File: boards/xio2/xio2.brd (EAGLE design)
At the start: 170 x 100 mm, 330 parts, among them J1 12401598E4#2A, Q1 BSS138, Q2 BSS138, Q3 BC817-16LT3G, Q4 BC817-16LT3G, X1 MINI-USB-UX60-MB-5ST, Y2 NX3225SA-12.000MHZ-STD-CSR-1

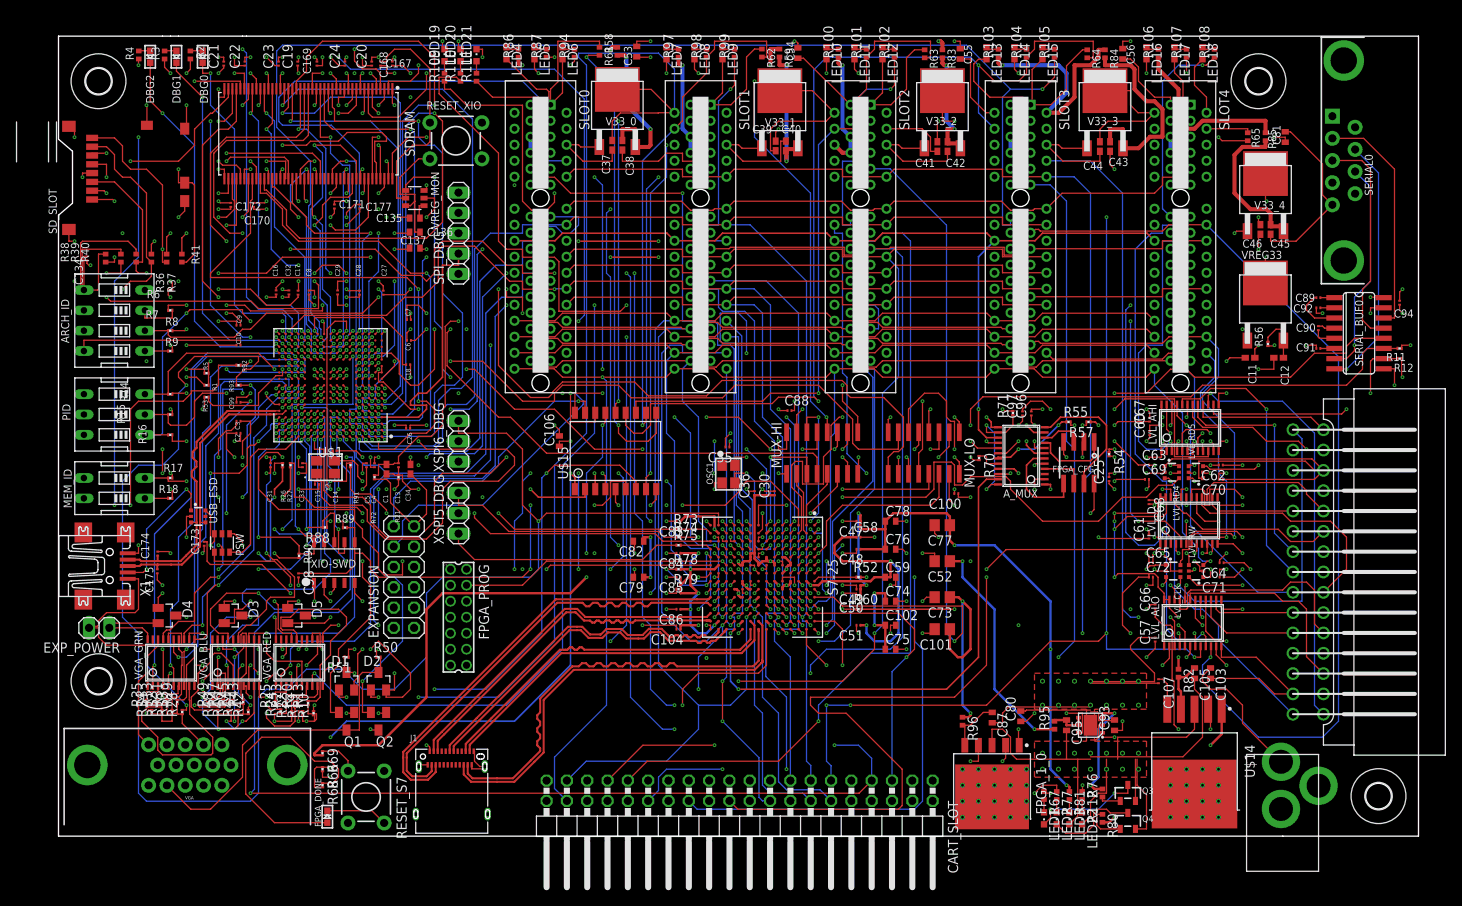
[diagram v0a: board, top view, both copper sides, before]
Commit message: Add slot signals between slots 1&2 and 3&4. Grounds on S5 Add capacitor to VBUS Removed the old annotations Changed resistors for STM debug leds Add pull-ups on TMDS inputs (TX lines on this schematic) Added ‘misc’ line to USB interface. Not high-speed.
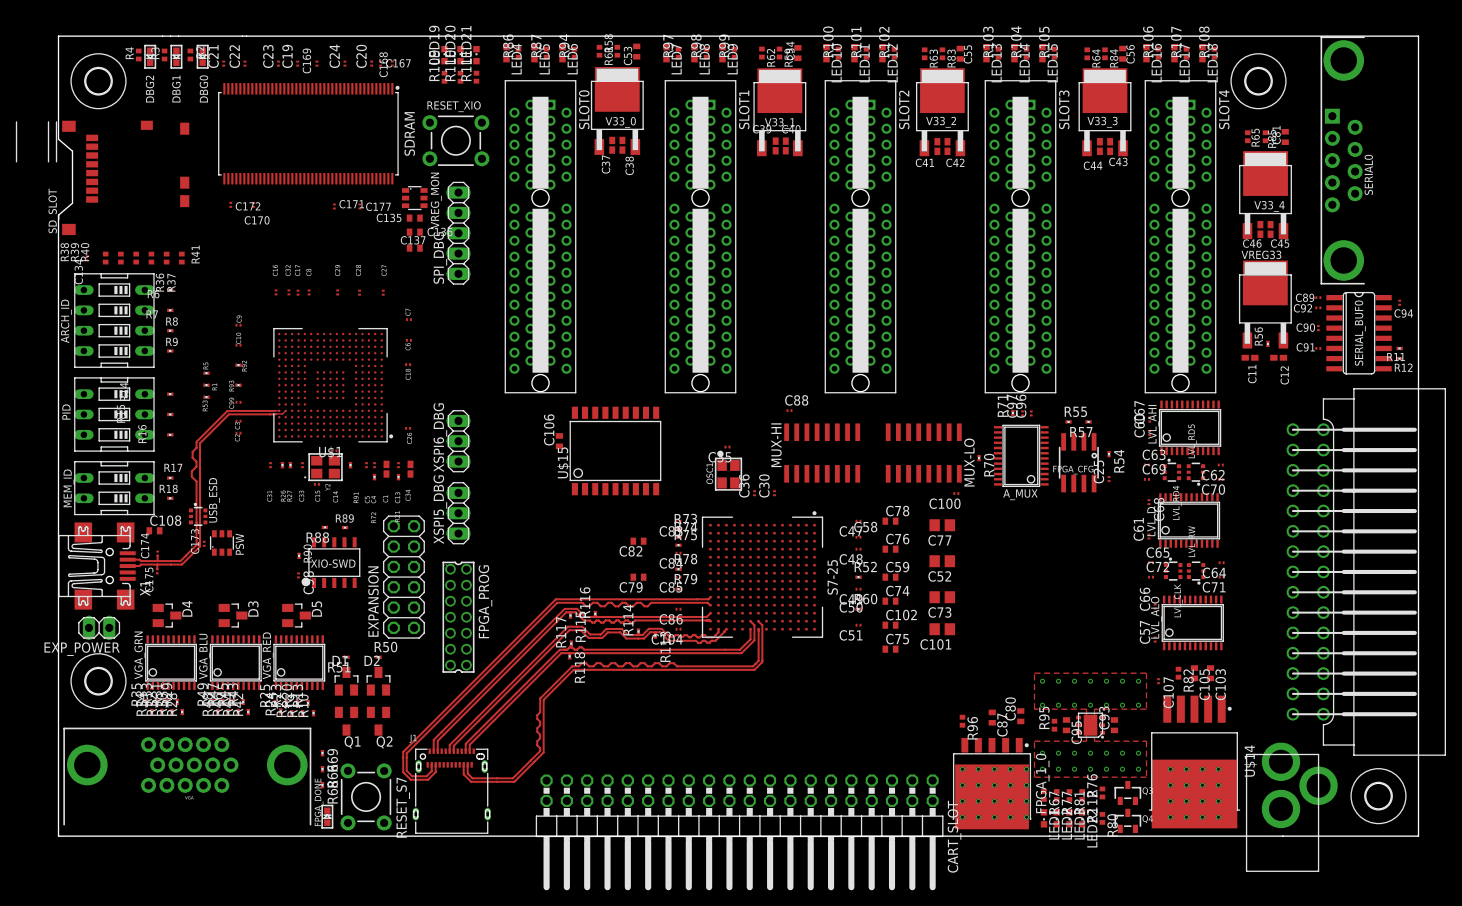
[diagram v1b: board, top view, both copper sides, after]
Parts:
- added C108: 4.7uF, rcl:C0402
- added R113, R114, R115, R116, R117, R118: 50R, rcl:R0201
- R2, R3, R4: value 1K -> 130R
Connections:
- new net LX_MISC: J1.A5, S7-25.M10
- new net SBUS12_CTL0: SLOT0.B8, SLOT1.B8
- new net SBUS12_CTL1: SLOT0.B9, SLOT1.B9
- new net SBUS12_CTL2: SLOT0.B10, SLOT1.B10
- new net SBUS12_CTL3: SLOT0.B11, SLOT1.B11
- new net SBUS12_CTL4: SLOT0.B12, SLOT1.B12
- new net SBUS12_D0: SLOT0.B18, SLOT1.B18
- new net SBUS12_D1: SLOT0.B19, SLOT1.B19
- new net SBUS12_D2: SLOT0.B20, SLOT1.B20
- new net SBUS12_D3: SLOT0.B21, SLOT1.B21
- new net SBUS12_D4: SLOT0.B22, SLOT1.B22
- new net SBUS12_D5: SLOT0.B23, SLOT1.B23
- new net SBUS12_D6: SLOT0.B24, SLOT1.B24
- new net SBUS12_D7: SLOT0.B25, SLOT1.B25
- new net SBUS34_CTL0: SLOT2.B8, SLOT3.B8
- new net SBUS34_CTL1: SLOT2.B9, SLOT3.B9
- new net SBUS34_CTL2: SLOT2.B10, SLOT3.B10
- new net SBUS34_CTL3: SLOT2.B11, SLOT3.B11
- new net SBUS34_CTL4: SLOT2.B12, SLOT3.B12
- new net SBUS34_D0: SLOT2.B18, SLOT3.B18
- new net SBUS34_D1: SLOT2.B19, SLOT3.B19
- new net SBUS34_D2: SLOT2.B20, SLOT3.B20
- new net SBUS34_D3: SLOT2.B21, SLOT3.B21
- new net SBUS34_D4: SLOT2.B22, SLOT3.B22
- new net SBUS34_D5: SLOT2.B23, SLOT3.B23
- new net SBUS34_D6: SLOT2.B24, SLOT3.B24
- new net SBUS34_D7: SLOT2.B25, SLOT3.B25
- net GND: now also C108.2, SLOT4.B10, SLOT4.B11, SLOT4.B12, SLOT4.B18, SLOT4.B19, SLOT4.B20, SLOT4.B21, SLOT4.B22, SLOT4.B23, SLOT4.B24, SLOT4.B25, SLOT4.B8, SLOT4.B9
- net LX_TC_N: now also R113.1
- net LX_TC_P: now also R114.1
- net LX_TD0_N: now also R115.1
- net LX_TD0_P: now also R116.1
- net LX_TD1_N: now also R117.1
- net LX_TD1_P: now also R118.1
- net VCCO: now also R113.2, R114.2, R115.2, R116.2, R117.2, R118.2
- net XIO_USB_VBUS: now also C108.1
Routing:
- net GND: track 970.2 -> 0.00 mm, vias 355 -> 64
- net +5V: track 683.6 -> 0.00 mm, vias 42 -> 0
- net HOST_A3: track 359.3 -> 0.00 mm, vias 7 -> 0
- net HOST_A15: track 345.9 -> 0.00 mm, vias 6 -> 0
- net +3V3: track 335.4 -> 0.00 mm, vias 138 -> 0
- net HOST_A7: track 316.5 -> 0.00 mm, vias 3 -> 0
- net HOST_A0: track 307.0 -> 0.00 mm, vias 5 -> 0
- net HOST_A1: track 294.7 -> 0.00 mm, vias 5 -> 0
- net HOST_A4: track 289.7 -> 0.00 mm, vias 5 -> 0
- net HOST_A6: track 279.7 -> 0.00 mm, vias 3 -> 0
- net SPI_CLK: track 278.7 -> 0.00 mm, vias 7 -> 0
- net HOST_A5: track 274.6 -> 0.00 mm, vias 7 -> 0
- net HOST_A11: track 265.5 -> 0.00 mm, vias 6 -> 0
- net HOST_A2: track 262.9 -> 0.00 mm, vias 6 -> 0
- net VCCO: track 261.9 -> 0.00 mm, vias 20 -> 0
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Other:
- board text removed: "USB3 connector uses milling layer for oval hole. Check this is valid"

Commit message: Change the input clock to 25MHz for STM. This is based on STM32Cube calculations
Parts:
- C14, C15: value 12pF -> 16pF
- Y2: value NX3225SA-12.000MHZ-STD-CSR-1 -> FA-238 25.0000MB-K3
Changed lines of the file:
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@@
 <attribute name="VALUE" x="43.95" y="46.5" size="1.016" layer="27" rot="R90"/>
 </element>
-<element name="Y2" library="microbuilder" package="CRYSTAL_3.2X2.5" value="NX3225SA-12.000MHZ-STD-CSR-1" x="33.3825" y="46.755" smashed="yes">
+<element name="Y2" library="microbuilder" package="CRYSTAL_3.2X2.5" value="FA-238 25.0000MB-K3" x="33.3825" y="46.755" smashed="yes">
 <attribute name="NAME" x="33.36925" y="44.73075" size="0.6096" layer="25" ratio="20" rot="R270"/>
 <attribute name="VALUE" x="31.4775" y="44.596" size="0.4064" layer="27" ratio="10"/>
 </element>
-<element name="C14" library="rcl" library_urn="urn:adsk.eagle:library:334" package="C0201" package3d_urn="urn:adsk.eagle:package:23690/2" value="12pF" x="34.5" y="48.8" smashed="yes">
+<element name="C14" library="rcl" library_urn="urn:adsk.eagle:library:334" package="C0201" package3d_urn="urn:adsk.eagle:package:23690/2" value="16pF" x="34.5" y="48.8" smashed="yes">
 <attribute name="NAME" x="34.93875" y="42.3" size="0.6096" layer="25" ratio="20" rot="R90"/>
 <attribute name="SPICEPREFIX" value="C" x="34.5" y="48.8" size="1.778" layer="27" display="off"/>
 <attribute name="VALUE" x="34" y="47.35" size="1.016" layer="27"/>
 </element>
-<element name="C15" library="rcl" library_urn="urn:adsk.eagle:library:334" package="C0201" package3d_urn="urn:adsk.eagle:package:23690/2" value="12pF" x="32.3" y="44.6" smashed="yes">
+<element name="C15" library="rcl" library_urn="urn:adsk.eagle:library:334" package="C0201" package3d_urn="urn:adsk.eagle:package:23690/2" value="16pF" x="32.3" y="44.6" smashed="yes">
 <attribute name="NAME" x="32.7" y="42.4" size="0.6096" layer="25" ratio="20" rot="R90"/>
 <attribute name="SPICEPREFIX" value="C" x="32.3" y="44.6" size="1.778" layer="27" display="off"/>

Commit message: Latest schematic and routed board
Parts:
- moved C15 20.2 mm to (47.2, 58.3), turned to 90 degrees
- moved Y2 14.9 mm to (44.2, 57.0), turned to 180 degrees
- moved C14 10.1 mm to (42.7, 54.7)
- moved R53 0.18 mm to (18.7, 55.5)
- moved R5 0.10 mm to (18.4, 58.5)
- moved C99 0.09 mm to (22.4, 54.9)
- renumbered CART_SLOT to HOST_IO, U$1 to XIO, X1 to USB
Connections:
- net N$1 renamed XIO_CLK_OUT
- net N$2 renamed XIO_CLK_IN
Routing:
- net GND: track 0.00 -> 793.6 mm, vias 64 -> 347
- net +5V: track 0.00 -> 594.1 mm, vias 0 -> 47
- net HOST_A3: track 0.00 -> 362.8 mm, vias 0 -> 6
- net HOST_A7: track 0.00 -> 329.8 mm, vias 0 -> 6
- net HOST_A6: track 0.00 -> 316.2 mm, vias 0 -> 6
- net HOST_A5: track 0.00 -> 311.9 mm, vias 0 -> 7
- net HOST_A2: track 0.00 -> 307.4 mm, vias 0 -> 4
- net HOST_A0: track 0.00 -> 301.0 mm, vias 0 -> 7
- net HOST_A10: track 0.00 -> 295.2 mm, vias 0 -> 10
- net HOST_A4: track 0.00 -> 284.1 mm, vias 0 -> 6
- net MCU_TX: track 0.00 -> 282.2 mm, vias 0 -> 3
- net HOST_A14: track 0.00 -> 270.9 mm, vias 0 -> 8
- net HOST_A8: track 0.00 -> 266.2 mm, vias 0 -> 7
- net VCCO: track 0.00 -> 262.6 mm, vias 0 -> 28
- net HOST_A12: track 0.00 -> 262.5 mm, vias 0 -> 7
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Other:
- board text added: "Xio -2- © 2018 SjG"
- board text removed: "TX:4mm RX: 6mm"

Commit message: Update some BOM-related things
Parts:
- C105, C93, C95: device rcl:C0402 -> rcl:C0402K
- C177: device rcl:C0201 -> rcl:C0402
- CARTRIDGE: value A8_CART -> 5650118-1
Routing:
- net LX_MISC: track 53.2 -> 55.0 mm
- net HOST_A0: track 301.0 -> 301.8 mm
- net VCCO: track 262.6 -> 261.9 mm

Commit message: Some small notes on layout
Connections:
- net N$72 renamed XSPI5_MISO_R
- net N$73 renamed XSPI5_MOSI_R
- net N$74 renamed XSPI5_SCK_R
- net N$75 renamed XSPI6_MISO_R
- net N$79 renamed XSPI6_SCK_R
- net N$98 renamed XSPI6_MOSI_R
- net XPSI5_MOSI renamed XSPI5_MOSI
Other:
- board text added: "1 : Signal 2 : GND 3 : Signal 14 : +5v / signal 15 : +3.3v 16 : Signal"
- board text added: "Add vias on 5v->3.3v vreg pads Play with cap/resistor placement on vregs Amrith recommends matched 3.3v and 5v caps to GND along 5v power plane border Move R91 to RHS of STM Move R92, R93 to bottom of STM"
- board text removed: "1 : Signal 2 : GND 3 : Signal 14 : +5v 15 : +3.3v 16 : Signal"
- board text removed: "1mm max len diff"
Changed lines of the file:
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@@
 <wire x1="23" y1="100.635" x2="23.5" y2="100.635" width="0" layer="20"/>
 <wire x1="23.5" y1="100.635" x2="170" y2="100.635" width="0" layer="20"/>
-<text x="142.5575" y="88.9" size="1.016" layer="48" ratio="15" rot="R180">1mm max
-len diff</text>
 <wire x1="0" y1="100.635" x2="0" y2="87.75" width="0" layer="20"/>
 <wire x1="0" y1="87.75" x2="1.75" y2="86.25" width="0" layer="20"/>
@@
 <wire x1="1.75" y1="79.75" x2="0" y2="78.25" width="0" layer="20"/>
 <wire x1="0" y1="78.25" x2="0" y2="0.635" width="0" layer="20"/>
-<text x="179.8736" y="82.422" size="1.016" layer="48" ratio="15">1   : Signal
+<text x="160.9236" y="-9.978" size="1.016" layer="48" ratio="10">1   : Signal
 2   : GND
 3   : Signal
-14 : +5v
+14 : +5v / signal
 15 : +3.3v
 16 : Signal</text>
@@
 <wire x1="132.425" y1="26.575" x2="117.35" y2="26.575" width="0.2" layer="25"/>
 <wire x1="117.35" y1="26.575" x2="117.35" y2="33.675" width="0.2" layer="25"/>
+<text x="28.2236" y="-12.703" size="1.016" layer="48" ratio="10">Add vias on 5v-&gt;3.3v vreg pads
+Play with cap/resistor placement on vregs
+Amrith recommends matched 3.3v and 5v caps to GND along 5v power plane border
+Move R91 to RHS of STM
+Move R92, R93 to bottom of STM</text>
 </plain>
 <attributes>
@@
 <wire x1="22.675" y1="55.45" x2="22.65" y2="55.475" width="0.1016" layer="1"/>
 </signal>
-<signal name="N$79" class="11">
+<signal name="XSPI6_SCK_R" class="11">
 <contactref element="R92" pad="1"/>
 <contactref element="XIO" pad="D9"/>
@@
 <via x="34.4" y="52.6" extent="1-16" drill="0.2" diameter="0.4794"/>
 </signal>
-<signal name="N$98" class="11">
+<signal name="XSPI6_MOSI_R" class="11">
 <contactref element="R93" pad="1"/>
 <contactref element="XIO" pad="D8"/>
@@
 <via x="37.6" y="62.2" extent="1-16" drill="0.2" diameter="0.4794"/>
 </signal>
-<signal name="N$72" class="11">
+<signal name="XSPI5_MISO_R" class="11">
 <contactref element="R91" pad="1"/>
 <contactref element="XIO" pad="K4"/>
@@
 <via x="86" y="39" extent="1-16" drill="0.2" diameter="0.4794"/>
 </signal>
-<signal name="N$73" class="11">
+<signal name="XSPI5_MOSI_R" class="11">
 <contactref element="R74" pad="2"/>
 <contactref element="S7-25" pad="L3"/>
@@
 <via x="84" y="38" extent="1-16" drill="0.2" diameter="0.4794"/>
 </signal>
-<signal name="N$74" class="11">
+<signal name="XSPI5_SCK_R" class="11">
 <contactref element="R75" pad="2"/>
 <contactref element="S7-25" pad="P4"/>
@@
 <via x="81" y="37" extent="1-16" drill="0.2" diameter="0.4794"/>
 </signal>
-<signal name="N$75" class="11">
+<signal name="XSPI6_MISO_R" class="11">
 <contactref element="R73" pad="2"/>
 <contactref element="S7-25" pad="P2"/>
@@
 <via x="81" y="39" extent="1-16" drill="0.2" diameter="0.4794"/>
 </signal>
-<signal name="XPSI5_MOSI" class="11">
+<signal name="XSPI5_MOSI" class="11">
 <contactref element="R74" pad="1"/>
 <contactref element="XIO" pad="L4"/>

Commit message: Update the TI vreg
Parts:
- U$14: value TPS876 -> TPS78633DCQR
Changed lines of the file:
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@@
 <attribute name="VALUE" x="124.46" y="4.1275" size="1.27" layer="27" rot="R270"/>
 </element>
-<element name="U$14" library="sjg-power" package="TO170P1524X483-6" package3d_urn="urn:adsk.eagle:package:4768344/1" value="TPS876" x="142" y="10" smashed="yes" rot="R270">
+<element name="U$14" library="sjg-power" package="TO170P1524X483-6" package3d_urn="urn:adsk.eagle:package:4768344/1" value="TPS78633DCQR" x="142" y="10" smashed="yes" rot="R270">
 <attribute name="NAME" x="148.272" y="10" size="1.016" layer="25" ratio="15" rot="R270" align="bottom-center"/>
 <attribute name="VALUE" x="135.728" y="10" size="1.27" layer="27" rot="R270" align="top-center"/>

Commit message: Design review first changes
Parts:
- renumbered U$14 to FPGA_VCCO
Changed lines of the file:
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@@
 <attribute name="VALUE" x="124.46" y="4.1275" size="1.27" layer="27" rot="R270"/>
 </element>
-<element name="U$14" library="sjg-power" package="TO170P1524X483-6" package3d_urn="urn:adsk.eagle:package:4768344/1" value="TPS78633DCQR" x="142" y="10" smashed="yes" rot="R270">
+<element name="FPGA_VCCO" library="sjg-power" package="TO170P1524X483-6" package3d_urn="urn:adsk.eagle:package:4768344/1" value="TPS78633DCQR" x="142" y="10" smashed="yes" rot="R270">
 <attribute name="NAME" x="148.272" y="10" size="1.016" layer="25" ratio="15" rot="R270" align="bottom-center"/>
 <attribute name="VALUE" x="135.728" y="10" size="1.27" layer="27" rot="R270" align="top-center"/>
@@
 <via x="145" y="7" extent="1-16" drill="0.35" locked="yes"/>
 <via x="145" y="9" extent="1-16" drill="0.35" locked="yes"/>
-<contactref element="U$14" pad="6"/>
-<contactref element="U$14" pad="3"/>
+<contactref element="FPGA_VCCO" pad="6"/>
+<contactref element="FPGA_VCCO" pad="3"/>
 <contactref element="C107" pad="2"/>
 <contactref element="C103" pad="2"/>
@@
 <contactref element="R77" pad="1"/>
 <contactref element="C103" pad="1"/>
-<contactref element="U$14" pad="2"/>
+<contactref element="FPGA_VCCO" pad="2"/>
 <polygon width="0.1524" layer="14">
 <vertex x="110.5" y="-4.5"/>
@@
 <contactref element="C59" pad="1"/>
 <contactref element="R80" pad="2"/>
-<contactref element="U$14" pad="1"/>
+<contactref element="FPGA_VCCO" pad="1"/>
 <contactref element="R95" pad="1"/>
 <contactref element="S7-25" pad="F10"/>
@@
 <signal name="N$88">
 <contactref element="C107" pad="1"/>
-<contactref element="U$14" pad="5"/>
+<contactref element="FPGA_VCCO" pad="5"/>
 <wire x1="138.6" y1="14.45" x2="138.6" y2="16.5" width="0.1016" layer="1"/>
 <wire x1="138.6" y1="20.25" x2="138.6" y2="14.45" width="0.1016" layer="16"/>
@@
 <signal name="N$89" class="7">
 <contactref element="C105" pad="1"/>
-<contactref element="U$14" pad="4"/>
+<contactref element="FPGA_VCCO" pad="4"/>
 <contactref element="R82" pad="2"/>
 <wire x1="140" y1="20.5" x2="140.625" y2="20.5" width="0.3048" layer="1"/>

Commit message: Simple changes from design reviews completed.
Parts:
- added BOOT_MODE: 209-3MS, special:EDG-03
- added R119: 100K, rcl:R0201
- added R120, R121: 10K, rcl:R0201
- added R122, R123, R124, R128: 1K, rcl:R0201
- added R125, R126, R127: 47K, rcl:R0201
- C173: value 0.1uF -> 1uF
- moved C169 0.95 mm to (31.4, 97.2)
- moved C19 0.42 mm to (29.5, 97.2)
- moved C171 0.31 mm to (34.7, 79.5)
- moved R7 0.14 mm to (14.1, 66.4), turned to 0 degrees
- moved R9 0.13 mm to (14.1, 61.3)
- moved R8 0.13 mm to (14.1, 63.8)
- moved R6 0.13 mm to (14.1, 68.9), turned to 0 degrees
- moved R18 0.07 mm to (14.0, 42.8)
- moved R15 0.05 mm to (14.0, 53.3)
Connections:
- net SPI_IRQ renamed !SPI_IRQ!
- new net BOOT_M0: BOOT_MODE.1, R127.1, S7-25.M7
- new net BOOT_M1: BOOT_MODE.2, R126.1, S7-25.M8
- new net BOOT_M2: BOOT_MODE.3, R125.1, S7-25.M9
- new net N$11: ARCH_ID.5, ARCH_ID.6, ARCH_ID.7, ARCH_ID.8, R122.2
- new net N$2: R121.2, SDRAM.67
- new net N$48: MEM_ID.3, MEM_ID.4, R123.2
- new net N$49: PID.4, PID.5, PID.6, R124.2
- new net N$50: BOOT_MODE.4, BOOT_MODE.5, BOOT_MODE.6, R128.2
- new net N$7: R120.1, SDRAM.20
- net +3V3: now also R121.1, R122.1, R123.1, R124.1, R128.1; no longer ARCH_ID.5, ARCH_ID.6, ARCH_ID.7, ARCH_ID.8, LVL_RD4.5, LVL_RD5.5, MEM_ID.3, MEM_ID.4, MUX-HI.16, MUX-LO.16, PID.4, PID.5, PID.6, S7-25.M7, SDRAM.67
- net +5V: now also LVL_RD4.5, LVL_RD5.5, R119.1
- net GND: now also R120.2, R125.2, R126.2, R127.2; no longer S7-25.M8, S7-25.M9, SDRAM.20
- net N$65: now also R119.2
- net VCCO: now also MUX-HI.16, MUX-LO.16
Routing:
- net GND: track 794.0 -> 0.00 mm, vias 347 -> 64
- net +5V: track 594.2 -> 0.00 mm, vias 47 -> 0
- net HOST_A3: track 362.8 -> 0.00 mm, vias 6 -> 0
- net HOST_A7: track 329.8 -> 0.00 mm, vias 6 -> 0
- net HOST_A6: track 316.2 -> 0.00 mm, vias 6 -> 0
- net HOST_A5: track 311.9 -> 0.00 mm, vias 7 -> 0
- net HOST_A2: track 307.1 -> 0.00 mm, vias 4 -> 0
- net HOST_A0: track 301.8 -> 0.00 mm, vias 7 -> 0
- net HOST_A10: track 295.2 -> 0.00 mm, vias 10 -> 0
- net HOST_A4: track 284.1 -> 0.00 mm, vias 6 -> 0
- net MCU_TX: track 282.2 -> 0.00 mm, vias 3 -> 0
- net HOST_A14: track 270.9 -> 0.00 mm, vias 8 -> 0
- net HOST_A8: track 266.2 -> 0.00 mm, vias 7 -> 0
- net HOST_A12: track 262.5 -> 0.00 mm, vias 7 -> 0
- net VCCO: track 261.9 -> 0.00 mm, vias 28 -> 0
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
